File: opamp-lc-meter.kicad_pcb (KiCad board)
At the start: 2 copper layers, 62.2 x 34.3 mm, 18 parts, among them J1 Conn_01x04, J2 Conn_02x04_Counter_Clockwise, J3 Conn_02x04_Counter_Clockwise, J4 Conn_01x02, J5 Conn_01x02, U1 LM393

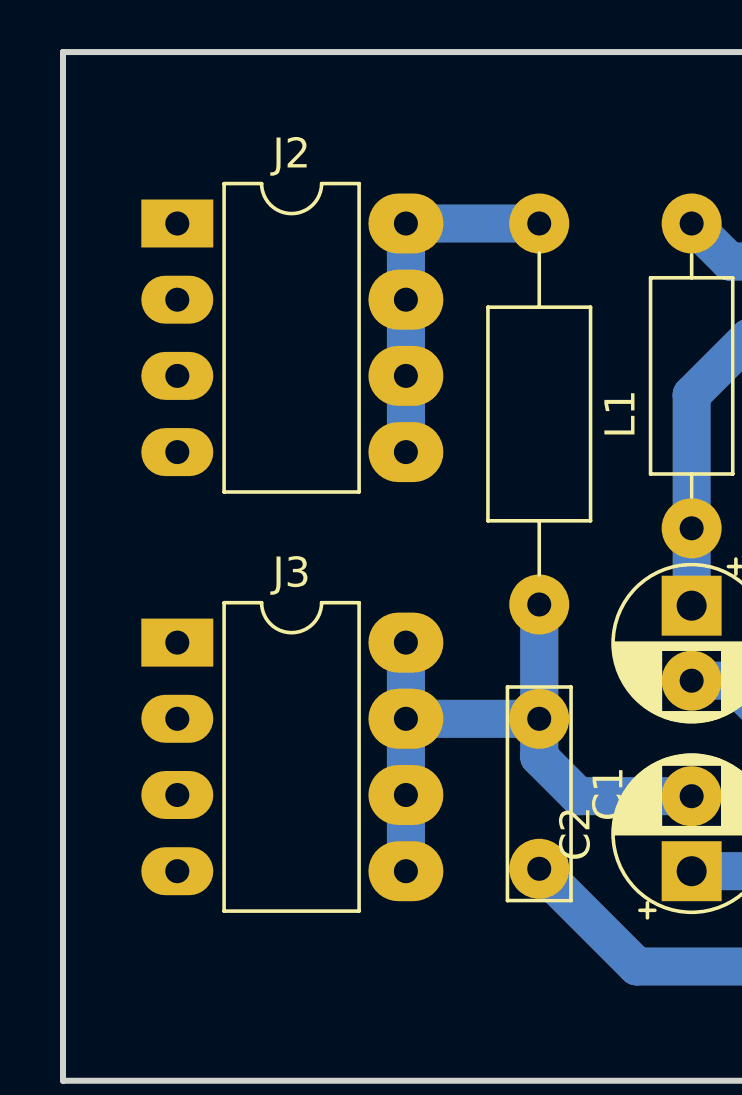
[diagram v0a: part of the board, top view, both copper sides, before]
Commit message: Change footprint of component socket to an actual socket
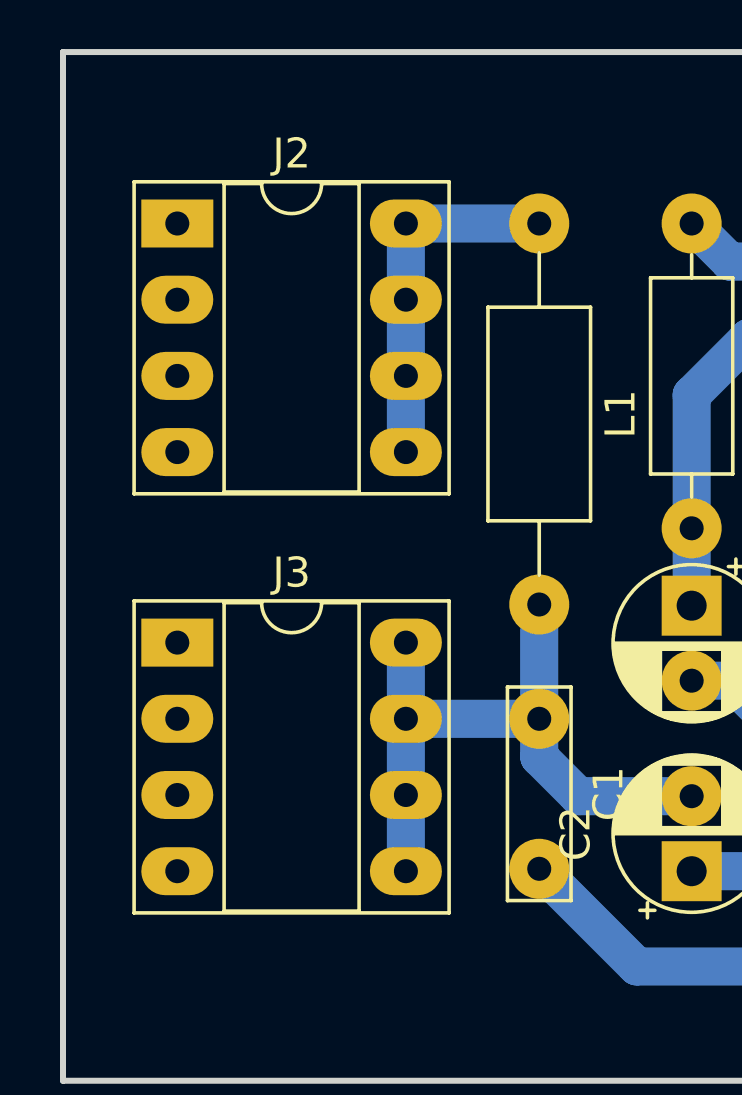
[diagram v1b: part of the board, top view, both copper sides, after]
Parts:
- J2, J3: footprint Package_DIP:DIP-8_W7.62mm_LongPads -> Package_DIP:DIP-8_W7.62mm_Socket_LongPads
